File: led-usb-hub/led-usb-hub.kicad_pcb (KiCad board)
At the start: 4 copper layers, 127 x 50.8 mm, 138 parts, among them J1 USBC_USB2.0, J2 RGBUSB_54-00266, J3 RGBUSB_54-00266, J4 RGBUSB_54-00266, J5 SWD, SW1 RESET, SW2 BOOLSEL, SW3 LED_EN, U1 RP2040, U10 TPD2EUSB30, U11 TPD2EUSB30, U12 TC54VN3002, U13 W25Q16JVSN, U2 TPS2042D, U3 TPS2042D, U4 TPS563257DRLR, U5 TPS563257DRLR, U6 TUSB2046IBVF, U7 TPD2EUSB30, U8 TPD2EUSB30, U9 TPD2EUSB30, Y1 12Mhz, Y2 6Mhz

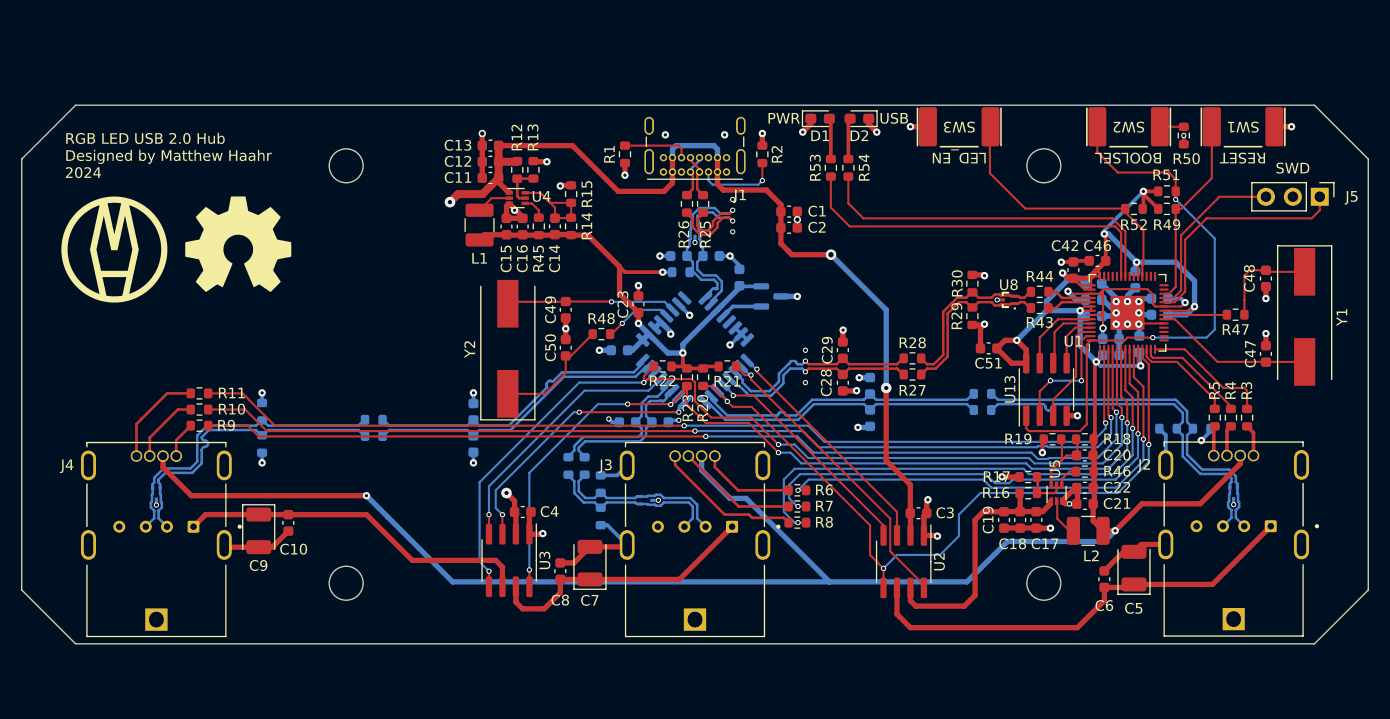
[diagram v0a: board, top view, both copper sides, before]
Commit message: Update Board to use #6 Screws
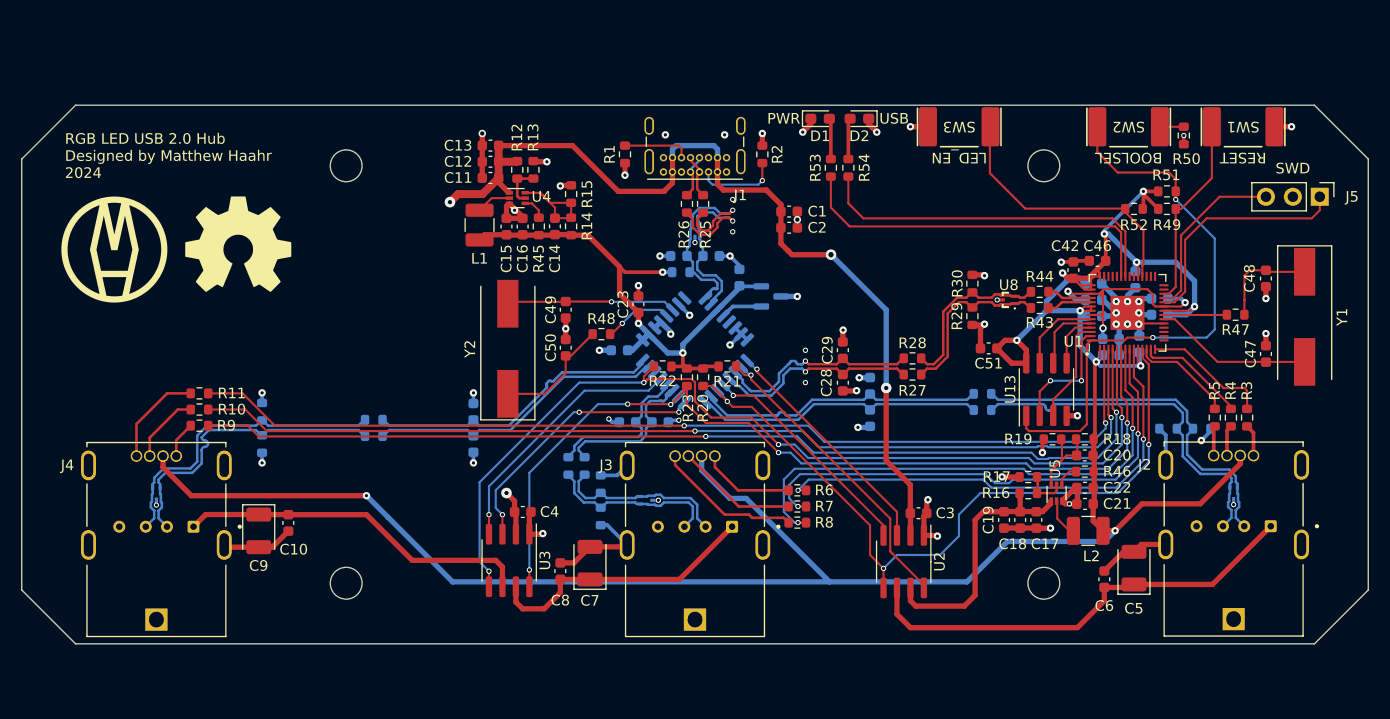
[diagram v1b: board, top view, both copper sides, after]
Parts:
- H1, H2, H3, H4: footprint MountingHole:MountingHole_3.2mm_M3 -> MountingHole:MountingHole_3mm
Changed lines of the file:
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@@
     )
   )
-  (footprint "MountingHole:MountingHole_3.2mm_M3" (layer "F.Cu")
+  (footprint "MountingHole:MountingHole_3mm" (layer "F.Cu")
     (at 64.128 126.873)
-    (descr "Mounting Hole 3.2mm, no annular, M3")
-    (tags "mounting hole 3.2mm no annular m3")
+    (descr "Mounting Hole 3mm, no annular")
+    (tags "mounting hole 3mm no annular")
     (property "Sheetfile" "led-usb-hub.kicad_sch")
     (property "Sheetname" "")
     (property "ki_description" "Mounting Hole without connection")
     (property "ki_keywords" "mounting hole")
+    (clearance 1)
     (attr exclude_from_pos_files)
-    (fp_text reference "H1" (at 0 -4.2) (layer "F.Fab")
+    (fp_text reference "H1" (at 0 -4) (layer "F.SilkS") hide
         (effects (font (size 1 1) (thickness 0.15)))
     )
-    (fp_text value "MountingHole" (at 0 1.152) (layer "F.Fab")
+    (fp_text value "MountingHole" (at 0 4) (layer "F.Fab")
         (effects (font (size 1 1) (thickness 0.15)))
     )
@@
         (effects (font (size 1 1) (thickness 0.15)))
     )
-    (fp_circle (center 0 0) (end 3.2 0)
+    (fp_circle (center 0 0) (end 3 0)
       (stroke (width 0.15) (type solid)) (fill none) (layer "Cmts.User"))
-    (fp_circle (center 0 0) (end 3.45 0)
+    (fp_circle (center 0 0) (end 3.25 0)
       (stroke (width 0.05) (type solid)) (fill none) (layer "F.CrtYd"))
-    (pad "" np_thru_hole circle (at 0 0) (size 3.2 3.2) (drill 3.2) (layers "F&B.Cu" "*.Mask")
-      (clearance 1))
+    (pad "" np_thru_hole circle (at 0 0) (size 3 3) (drill 3) (layers "*.Cu" "*.Mask"))
   )
   (footprint "KSS221GLFS:SW_KSS221GLFS" (layer "F.Cu")
@@
     )
   )
-  (footprint "MountingHole:MountingHole_3.2mm_M3" (layer "F.Cu")
+  (footprint "MountingHole:MountingHole_3mm" (layer "F.Cu")
     (at 129.928 87.503)
-    (descr "Mounting Hole 3.2mm, no annular, M3")
-    (tags "mounting hole 3.2mm no annular m3")
+    (descr "Mounting Hole 3mm, no annular")
+    (tags "mounting hole 3mm no annular")
     (property "Sheetfile" "led-usb-hub.kicad_sch")
     (property "Sheetname" "")
     (property "ki_description" "Mounting Hole without connection")
     (property "ki_keywords" "mounting hole")
+    (clearance 1)
     (attr exclude_from_pos_files)
-    (fp_text reference "H4" (at 0 -4.2) (layer "F.Fab")
+    (fp_text reference "H4" (at 0 -4) (layer "F.SilkS") hide
         (effects (font (size 1 1) (thickness 0.15)))
     )
-    (fp_text value "MountingHole" (at 0.381 4.2) (layer "F.Fab")
+    (fp_text value "MountingHole" (at 0 4) (layer "F.Fab")
         (effects (font (size 1 1) (thickness 0.15)))
     )
@@
         (effects (font (size 1 1) (thickness 0.15)))
     )
-    (fp_circle (center 0 0) (end 3.2 0)
+    (fp_circle (center 0 0) (end 3 0)
       (stroke (width 0.15) (type solid)) (fill none) (layer "Cmts.User"))
-    (fp_circle (center 0 0) (end 3.45 0)
+    (fp_circle (center 0 0) (end 3.25 0)
       (stroke (width 0.05) (type solid)) (fill none) (layer "F.CrtYd"))
-    (pad "" np_thru_hole circle (at 0 0) (size 3.2 3.2) (drill 3.2) (layers "F&B.Cu" "*.Mask")
-      (clearance 1))
+    (pad "" np_thru_hole circle (at 0 0) (size 3 3) (drill 3) (layers "*.Cu" "*.Mask"))
   )
   (footprint "Package_SO:SOIC-8_3.9x4.9mm_P1.27mm" (layer "F.Cu")
@@
     )
   )
-  (footprint "MountingHole:MountingHole_3.2mm_M3" (layer "F.Cu")
+  (footprint "MountingHole:MountingHole_3mm" (layer "F.Cu")
     (at 129.928 126.873)
-    (descr "Mounting Hole 3.2mm, no annular, M3")
-    (tags "mounting hole 3.2mm no annular m3")
+    (descr "Mounting Hole 3mm, no annular")
+    (tags "mounting hole 3mm no annular")
     (property "Sheetfile" "led-usb-hub.kicad_sch")
     (property "Sheetname" "")
     (property "ki_description" "Mounting Hole without connection")
     (property "ki_keywords" "mounting hole")
+    (clearance 1)
     (attr exclude_from_pos_files)
-    (fp_text reference "H2" (at 0.762 -9.66) (layer "F.Fab")
+    (fp_text reference "H2" (at 0 -4) (layer "F.SilkS") hide
         (effects (font (size 1 1) (thickness 0.15)))
     )
-    (fp_text value "MountingHole" (at -0.1405 -0.0045) (layer "F.Fab")
+    (fp_text value "MountingHole" (at 0 4) (layer "F.Fab")
         (effects (font (size 1 1) (thickness 0.15)))
     )
@@
         (effects (font (size 1 1) (thickness 0.15)))
     )
-    (fp_circle (center 0 0) (end 3.2 0)
+    (fp_circle (center 0 0) (end 3 0)
       (stroke (width 0.15) (type solid)) (fill none) (layer "Cmts.User"))
-    (fp_circle (center 0 0) (end 3.45 0)
+    (fp_circle (center 0 0) (end 3.25 0)
       (stroke (width 0.05) (type solid)) (fill none) (layer "F.CrtYd"))
-    (pad "" np_thru_hole circle (at 0 0) (size 3.2 3.2) (drill 3.2) (layers "F&B.Cu" "*.Mask")
-      (clearance 1))
+    (pad "" np_thru_hole circle (at 0 0) (size 3 3) (drill 3) (layers "*.Cu" "*.Mask"))
   )
   (footprint "Capacitor_SMD:C_0603_1608Metric" (layer "F.Cu")
@@
     )
   )
-  (footprint "MountingHole:MountingHole_3.2mm_M3" (layer "F.Cu")
+  (footprint "MountingHole:MountingHole_3mm" (layer "F.Cu")
     (at 64.128 87.503)
-    (descr "Mounting Hole 3.2mm, no annular, M3")
-    (tags "mounting hole 3.2mm no annular m3")
+    (descr "Mounting Hole 3mm, no annular")
+    (tags "mounting hole 3mm no annular")
     (property "Sheetfile" "led-usb-hub.kicad_sch")
     (property "Sheetname" "")
     (property "ki_description" "Mounting Hole without connection")
     (property "ki_keywords" "mounting hole")
+    (clearance 1)
     (attr exclude_from_pos_files)
-    (fp_text reference "H3" (at 0 -4.2) (layer "F.Fab")
+    (fp_text reference "H3" (at 0 -4) (layer "F.SilkS") hide
         (effects (font (size 1 1) (thickness 0.15)))
     )
-    (fp_text value "MountingHole" (at 0 4.2) (layer "F.Fab")
+    (fp_text value "MountingHole" (at 0 4) (layer "F.Fab")
         (effects (font (size 1 1) (thickness 0.15)))
     )
@@
         (effects (font (size 1 1) (thickness 0.15)))
     )
-    (fp_circle (center 0 0) (end 3.2 0)
+    (fp_circle (center 0 0) (end 3 0)
       (stroke (width 0.15) (type solid)) (fill none) (layer "Cmts.User"))
-    (fp_circle (center 0 0) (end 3.45 0)
+    (fp_circle (center 0 0) (end 3.25 0)
       (stroke (width 0.05) (type solid)) (fill none) (layer "F.CrtYd"))
-    (pad "" np_thru_hole circle (at 0 0) (size 3.2 3.2) (drill 3.2) (layers "F&B.Cu" "*.Mask")
-      (clearance 1))
+    (pad "" np_thru_hole circle (at 0 0) (size 3 3) (drill 3) (layers "*.Cu" "*.Mask"))
   )
   (footprint "Resistor_SMD:R_0603_1608Metric" (layer "F.Cu")
@@
   (gr_circle (center 98.298 98.806) (end 98.398 98.806)
     (stroke (width 0.15) (type solid)) (fill solid) (layer "B.SilkS"))
+  (gr_circle (center 134.0104 105.2576) (end 134.1104 105.2576)
+    (stroke (width 0.15) (type solid)) (fill solid) (layer "F.SilkS"))
   (gr_line (start 38.608 132.588) (end 155.448 132.588)
     (stroke (width 0.1) (type default)) (layer "Edge.Cuts"))

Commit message: Beautification
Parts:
- moved C48 4.50 mm to (150.9, 102.6)
- moved Y1 4.23 mm to (154.5, 106.0)
- moved C47 1.96 mm to (150.9, 107.2)
- moved SW3 0.63 mm to (122.6, 83.8)
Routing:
- net Net-(C48-Pad1): track 9.64 -> 5.93 mm
- net Net-(U1-XIN): track 15.0 -> 16.7 mm
- net Earth: track 142.4 -> 143.8 mm, vias 64 -> 63
- net L1_R: track 12.0 -> 11.4 mm
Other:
- board text added: "DAT GND CLK"
- board text added: "USB-1"
- board text added: "USB-2"
- board text added: "USB-3"
- board text added: "USB-US"

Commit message: More beautification
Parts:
- moved R3 3.70 mm to (148.1, 107.7)
- moved R4 3.70 mm to (146.6, 107.7)
- moved R5 3.70 mm to (145.0, 107.7)
- moved R22 1.52 mm to (95.5, 106.4)
- moved R21 1.52 mm to (98.6, 106.4)
- moved R10 1.46 mm to (51.8, 110.5)
- moved R11 1.46 mm to (51.8, 109.0)
- moved R9 1.46 mm to (51.8, 112.0)
- moved R20 0.92 mm to (98.6, 108.0), turned to 180 degrees
- moved R23 0.92 mm to (95.5, 108.0), turned to 0 degrees
- moved C47 0.50 mm to (150.9, 107.7)
- moved C42 0.13 mm to (132.7, 97.2)
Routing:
- net Earth: track 143.8 -> 147.9 mm
- net Net-(J2-PadR): track 3.01 -> 6.99 mm
- net Net-(J2-PadB): track 2.80 -> 6.70 mm
- net Net-(J2-PadG): track 2.91 -> 6.58 mm
- net 3V3_L: track 51.5 -> 55.2 mm
- net L1_B: track 9.69 -> 6.72 mm
- net L1_R: track 11.4 -> 8.52 mm
- net L1_G: track 10.4 -> 8.20 mm
- net 3V3_PI: track 235.6 -> 237.2 mm
- net OC0: track 30.0 -> 31.6 mm
- net L3_B: track 94.6 -> 93.1 mm
- net L3_R: track 96.4 -> 94.9 mm
- net Net-(J4-PadR): track 3.43 -> 4.89 mm
- net Net-(J4-PadG): track 6.70 -> 8.16 mm
- net Net-(J4-PadB): track 9.34 -> 10.8 mm
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
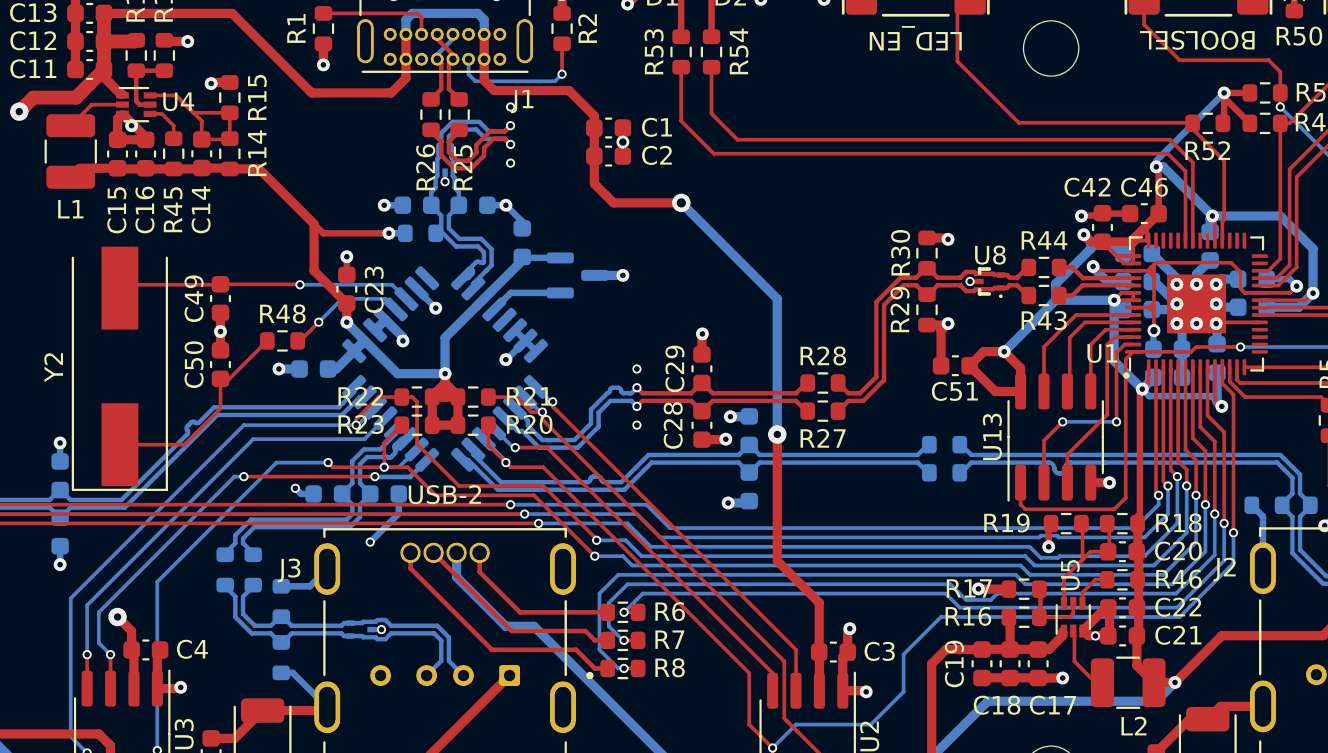
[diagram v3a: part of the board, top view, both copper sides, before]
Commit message: Clean up pad traces with zones
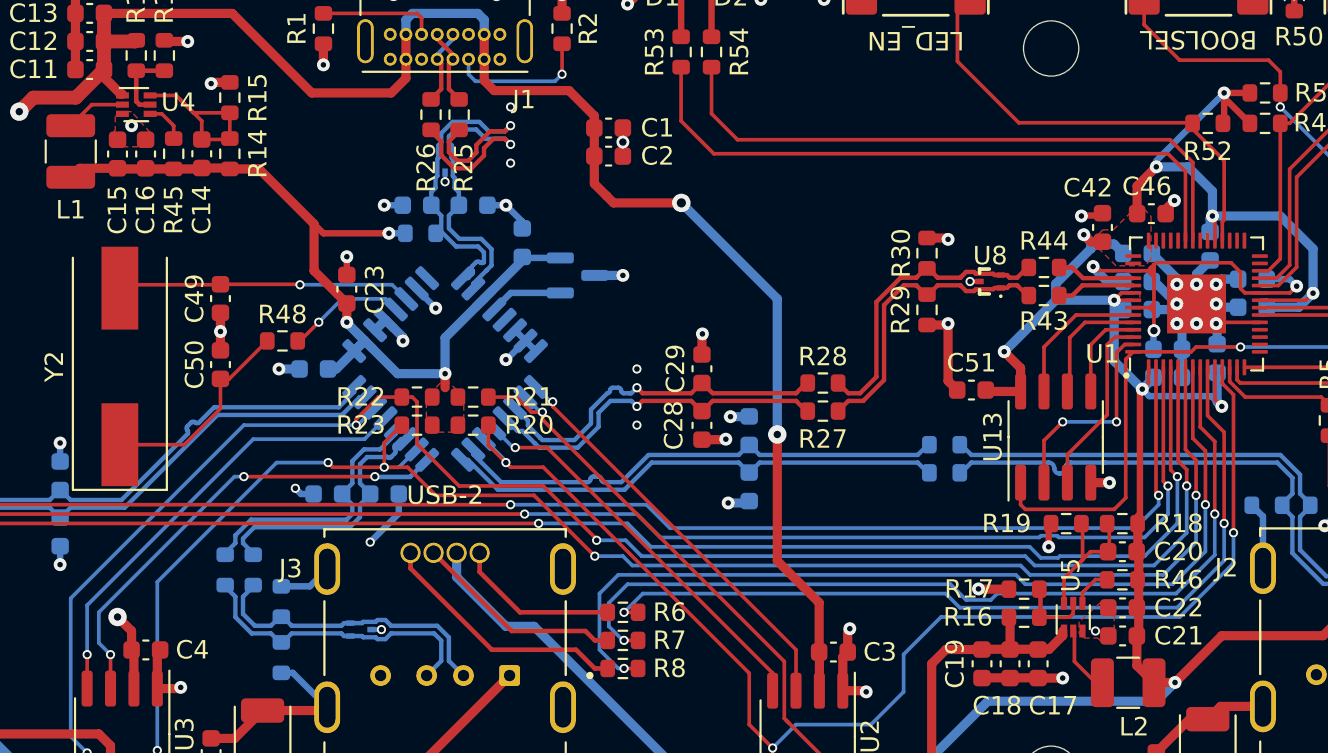
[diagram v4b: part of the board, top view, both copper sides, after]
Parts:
- moved C51 1.59 mm to (125.6, 106.0)
- moved C46 0.38 mm to (135.4, 96.5), turned to 0 degrees
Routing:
- net 3V3_PI: track 237.2 -> 222.9 mm
- net Earth: track 147.9 -> 138.8 mm, vias 63 -> 64
- net 3V3_L: track 55.2 -> 46.9 mm
- added copper zone on F.Cu, net 3V3_L
- added copper zone on F.Cu, net 3V3_PI
- added copper zone on F.Cu, net Earth

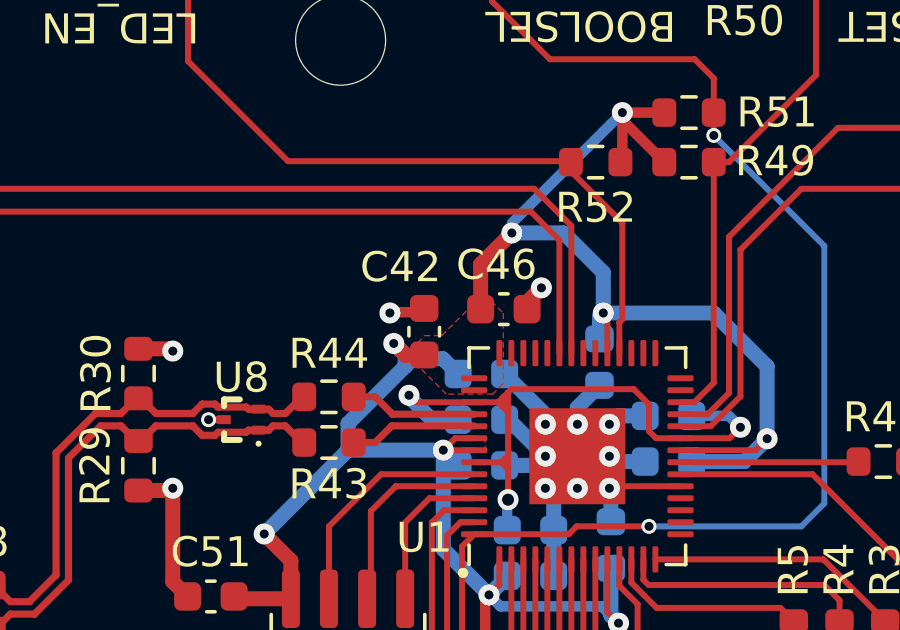
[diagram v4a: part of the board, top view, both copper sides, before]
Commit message: Add Teardrops
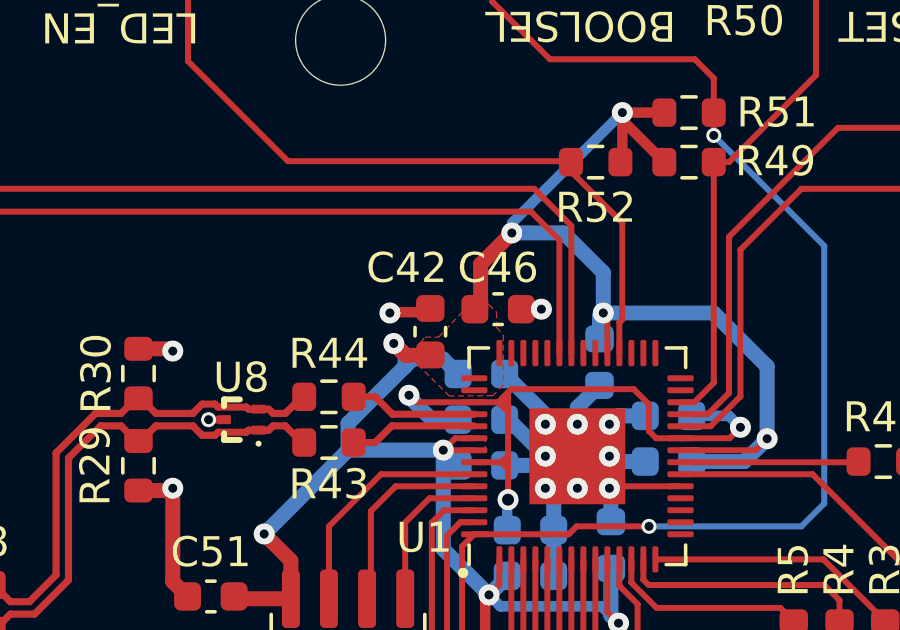
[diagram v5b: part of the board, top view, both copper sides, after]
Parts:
- moved C42 0.20 mm to (132.9, 97.2)
- moved C46 0.19 mm to (135.2, 96.5)
